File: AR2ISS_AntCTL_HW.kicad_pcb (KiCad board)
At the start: 2 copper layers, 160 x 111.5 mm, 226 parts, among them J1 Conn_01x02, J10 Conn_01x02, J11 Conn_01x02, J12 Conn_01x02, J13 Conn_01x02, J2 Conn_01x04, J3 Conn_02x17_Odd_Even, J4 Conn_02x17_Odd_Even, J5 Conn_02x03_Odd_Even, J6 Conn_01x10, J7 DB9_Female, J8 Conn_01x02, J9 RJ45_LED, K1 G6S-2, Q1 AO3400A, Q2 APM4953KC, Q3 AO3400A, Q4 AO3400A, Q5 AO3400A, Q6 AO3400A, Q7 AO3400A, Q8 AO3400A, Q9 AO3400A, U1 non_plated, U10 74HC164, U11 MCP23017_SO, U12 STM32L522CCTx, U13 SN75176AD, U14 SN75176AD, U15 SN75176AD, U16 SN75176AD, U2 non_plated, U3 non_plated, U4 non_plated, U5 LME78_05-1.0, U6 L78033, U7 TSC101B, U8 MCP23017_SO, U9 TXB0102DCT, Y1 8M

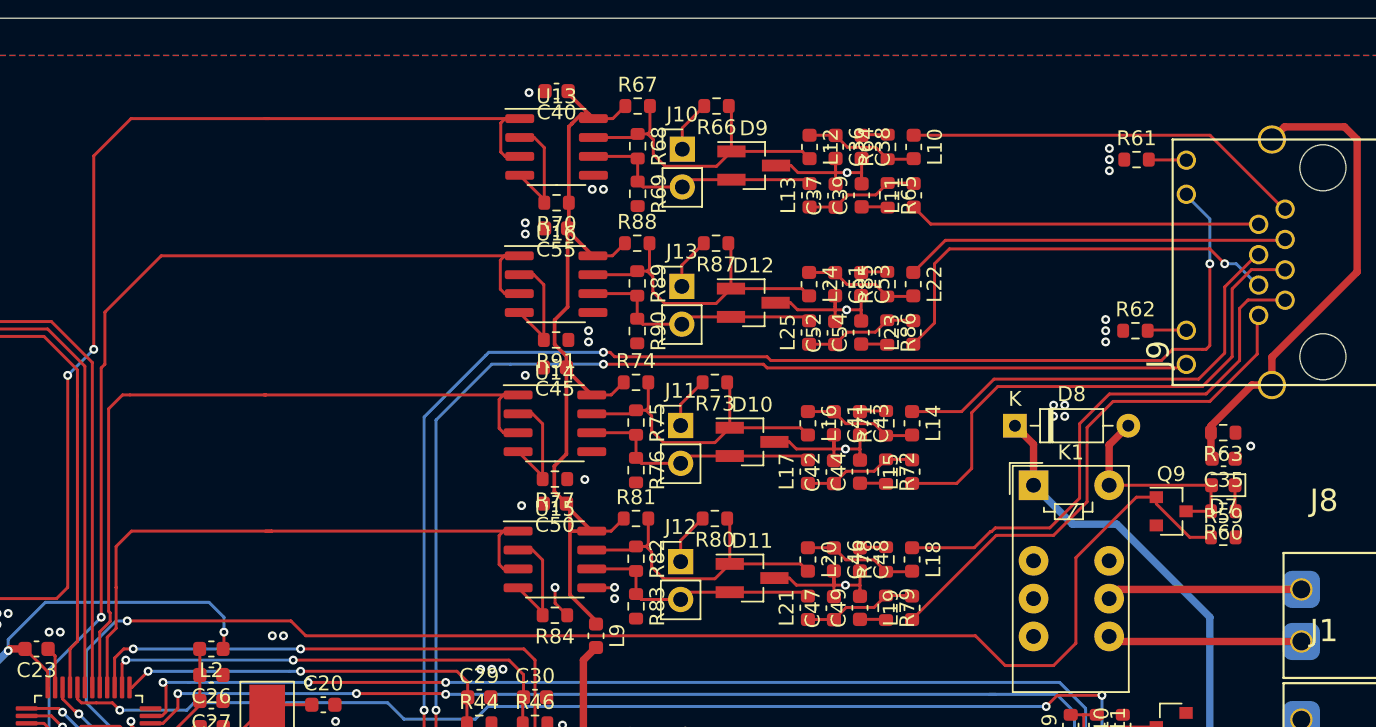
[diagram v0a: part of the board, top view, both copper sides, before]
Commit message: rx tx fix, filter mirrored
switched rx/tx signals
filters were mirrored
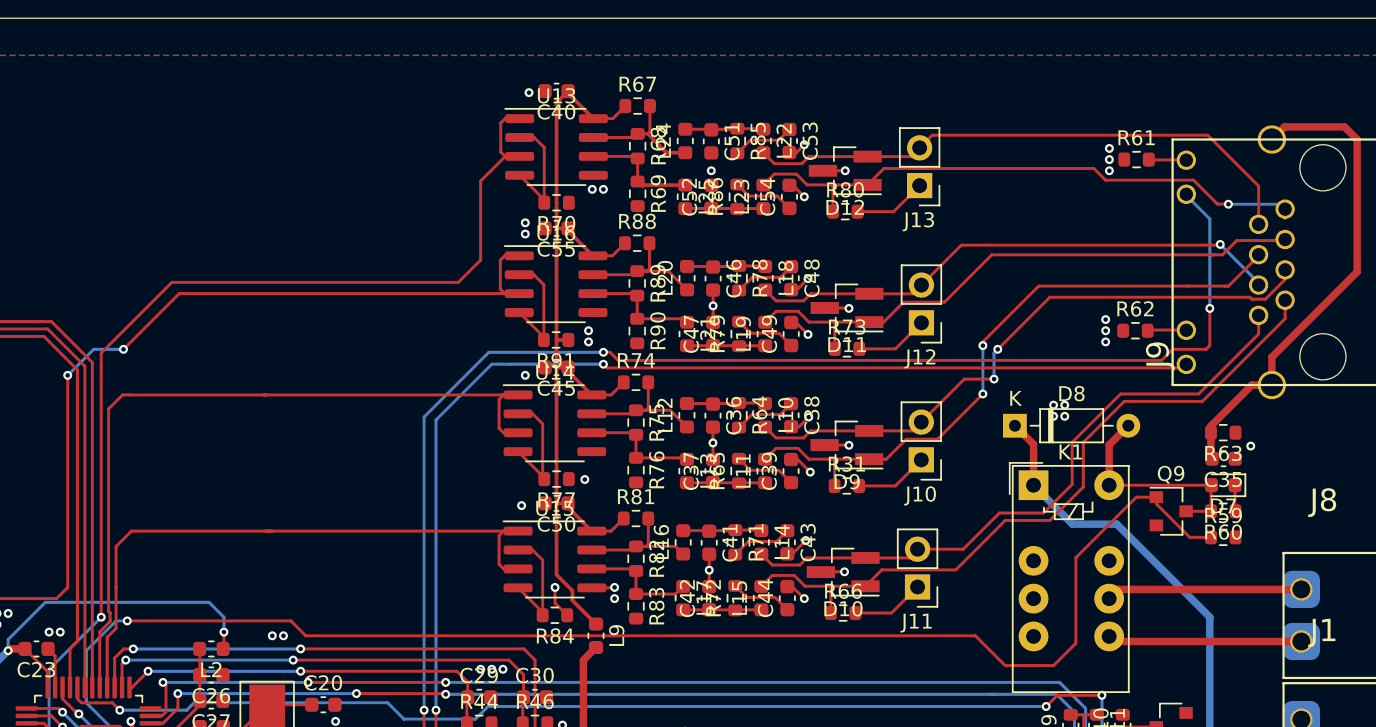
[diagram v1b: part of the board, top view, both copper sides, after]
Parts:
- removed R87: 120, Resistor_SMD:R_0603_1608Metric
- added R31: 120, Resistor_SMD:R_0603_1608Metric, F.Cu at (163.4, 69.9)
- L10, L11, L14, L15, L18, L19, L22, L23: value 10u -> 74279266
- L12, L13, L16, L17, L20, L21, L24, L25: value 74279266 -> 10u
- R64, R65, R71, R72, R78, R79, R85, R86: value 221 -> 220
- moved R66 35.1 mm to (163.1, 78.5), turned to 0 degrees
- moved J10 26.3 mm to (168.4, 68.2), turned to 180 degrees
- moved J12 22.8 mm to (168.4, 59.0), turned to 180 degrees
- moved R80 22.4 mm to (163.2, 51.5), turned to 0 degrees
- moved L18 21.3 mm to (157.9, 56.0)
- moved R78 21.3 mm to (156.1, 56.0), turned to 270 degrees
- moved L11 21.1 mm to (157.9, 68.9)
- moved R65 21.1 mm to (156.1, 68.9), turned to 90 degrees
- moved L19 20.9 mm to (157.9, 59.7)
- moved R79 20.9 mm to (156.1, 59.7), turned to 90 degrees
- moved L10 20.6 mm to (157.9, 65.2)
- moved R64 20.6 mm to (156.1, 65.2), turned to 270 degrees
- moved L20 20.6 mm to (152.6, 56.0), turned to 90 degrees
- moved C46 20.5 mm to (154.4, 56.0)
- moved L13 20.3 mm to (152.6, 68.9), turned to 270 degrees
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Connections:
- C40 pad 1: /RS422/RS485Tranceiver1/MODE -> /RS422/RS485Tranceiver2/MODE
- C45 pad 1: /RS422/RS485Tranceiver1/MODE -> /RS422/RS485Tranceiver2/MODE
- C50 pad 1: /RS422/RS485Tranceiver1/MODE -> /RS422/RS485Tranceiver2/MODE
- C55 pad 1: /RS422/RS485Tranceiver1/MODE -> /RS422/RS485Tranceiver2/MODE
- D10 pad 1: Net-(D10-Pad1) -> /RS422/RS485Tranceiver4/A_in
- D10 pad 2: Net-(D10-Pad2) -> /RS422/RS485Tranceiver4/B_in
- D11 pad 1: Net-(D11-Pad1) -> /RS422/RS485Tranceiver2/A_in
- D11 pad 2: Net-(D11-Pad2) -> /RS422/RS485Tranceiver2/B_in
- D12 pad 1: Net-(D12-Pad1) -> /RS422/RS485Tranceiver1/A_in
- D12 pad 2: Net-(D12-Pad2) -> /RS422/RS485Tranceiver1/B_in
- D9 pad 1: Net-(D9-Pad1) -> /RS422/RS485Tranceiver3/A_in
- D9 pad 2: Net-(D9-Pad2) -> /RS422/RS485Tranceiver3/B_in
- J10 pad 2: Net-(D9-Pad2) -> /RS422/RS485Tranceiver3/B_in
- J11 pad 2: Net-(D10-Pad2) -> /RS422/RS485Tranceiver4/B_in
- J12 pad 2: Net-(D11-Pad2) -> /RS422/RS485Tranceiver2/B_in
- J13 pad 2: Net-(D12-Pad2) -> /RS422/RS485Tranceiver1/B_in
- L10 pad 1: /RS422/RS485Tranceiver1/A_in -> Net-(C36-Pad1)
- L10 pad 2: Net-(C36-Pad1) -> /RS422/RS485Tranceiver3/B_in
- L11 pad 1: /RS422/RS485Tranceiver1/B_in -> Net-(C37-Pad1)
- L11 pad 2: Net-(C37-Pad1) -> /RS422/RS485Tranceiver3/A_in
- L12 pad 1: Net-(C36-Pad1) -> /RS422/RS485Tranceiver3/filter/A_Out
- L12 pad 2: Net-(D9-Pad1) -> Net-(C36-Pad1)
- L13 pad 1: Net-(C37-Pad1) -> /RS422/RS485Tranceiver3/filter/B_Out
- L13 pad 2: Net-(D9-Pad2) -> Net-(C37-Pad1)
- L14 pad 1: /RS422/RS485Tranceiver3/A_in -> Net-(C41-Pad1)
- L14 pad 2: Net-(C41-Pad1) -> /RS422/RS485Tranceiver4/B_in
- L15 pad 1: /RS422/RS485Tranceiver3/B_in -> Net-(C42-Pad1)
- L15 pad 2: Net-(C42-Pad1) -> /RS422/RS485Tranceiver4/A_in
- L16 pad 1: Net-(C41-Pad1) -> /RS422/RS485Tranceiver4/filter/A_Out
- L16 pad 2: Net-(D10-Pad1) -> Net-(C41-Pad1)
- L17 pad 1: Net-(C42-Pad1) -> /RS422/RS485Tranceiver4/filter/B_Out
- L17 pad 2: Net-(D10-Pad2) -> Net-(C42-Pad1)
- L18 pad 1: /RS422/RS485Tranceiver4/A_in -> Net-(C46-Pad1)
- L18 pad 2: Net-(C46-Pad1) -> /RS422/RS485Tranceiver2/B_in
- L19 pad 1: /RS422/RS485Tranceiver4/B_in -> Net-(C47-Pad1)
- L19 pad 2: Net-(C47-Pad1) -> /RS422/RS485Tranceiver2/A_in
- L20 pad 1: Net-(C46-Pad1) -> /RS422/RS485Tranceiver2/filter/A_Out
- L20 pad 2: Net-(D11-Pad1) -> Net-(C46-Pad1)
- L21 pad 1: Net-(C47-Pad1) -> /RS422/RS485Tranceiver2/filter/B_Out
- L21 pad 2: Net-(D11-Pad2) -> Net-(C47-Pad1)
- L22 pad 1: /RS422/RS485Tranceiver2/A_in -> Net-(C51-Pad1)
- L22 pad 2: Net-(C51-Pad1) -> /RS422/RS485Tranceiver1/B_in
- L23 pad 1: /RS422/RS485Tranceiver2/B_in -> Net-(C52-Pad1)
- L23 pad 2: Net-(C52-Pad1) -> /RS422/RS485Tranceiver1/A_in
- L24 pad 1: Net-(C51-Pad1) -> /RS422/RS485Tranceiver1/filter/A_Out
- L24 pad 2: Net-(D12-Pad1) -> Net-(C51-Pad1)
- L25 pad 1: Net-(C52-Pad1) -> /RS422/RS485Tranceiver1/filter/B_Out
- L25 pad 2: Net-(D12-Pad2) -> Net-(C52-Pad1)
- L9 pad 1: /RS422/RS485Tranceiver1/MODE -> /RS422/RS485Tranceiver2/MODE
- R66 pad 1: Net-(D9-Pad1) -> /RS422/RS485Tranceiver4/A_in
- R66 pad 2: Net-(J10-Pad1) -> Net-(J11-Pad1)
- R67 pad 1: /RS422/RS485Tranceiver1/MODE -> /RS422/RS485Tranceiver2/MODE
- R67 pad 2: Net-(D9-Pad1) -> /RS422/RS485Tranceiver1/filter/A_Out
- R68 pad 1: Net-(D9-Pad1) -> /RS422/RS485Tranceiver1/filter/A_Out
- R68 pad 2: Net-(D9-Pad2) -> /RS422/RS485Tranceiver1/filter/B_Out
- R69 pad 1: Net-(D9-Pad2) -> /RS422/RS485Tranceiver1/filter/B_Out
- R70 pad 1: /RS422/RS485Tranceiver1/MODE -> GND
- R73 pad 1: Net-(D10-Pad1) -> /RS422/RS485Tranceiver2/A_in
- R73 pad 2: Net-(J11-Pad1) -> Net-(J12-Pad1)
- R74 pad 1: /RS422/RS485Tranceiver1/MODE -> /RS422/RS485Tranceiver2/MODE
- R74 pad 2: Net-(D10-Pad1) -> /RS422/RS485Tranceiver3/filter/A_Out
- R75 pad 1: Net-(D10-Pad1) -> /RS422/RS485Tranceiver3/filter/A_Out
- R75 pad 2: Net-(D10-Pad2) -> /RS422/RS485Tranceiver3/filter/B_Out
- R76 pad 1: Net-(D10-Pad2) -> /RS422/RS485Tranceiver3/filter/B_Out
- R80 pad 1: Net-(D11-Pad1) -> /RS422/RS485Tranceiver1/A_in
- R80 pad 2: Net-(J12-Pad1) -> Net-(J13-Pad1)
- R81 pad 1: /RS422/RS485Tranceiver1/MODE -> /RS422/RS485Tranceiver2/MODE
- R81 pad 2: Net-(D11-Pad1) -> /RS422/RS485Tranceiver4/filter/A_Out
- R82 pad 1: Net-(D11-Pad1) -> /RS422/RS485Tranceiver4/filter/A_Out
- R82 pad 2: Net-(D11-Pad2) -> /RS422/RS485Tranceiver4/filter/B_Out
- R83 pad 1: Net-(D11-Pad2) -> /RS422/RS485Tranceiver4/filter/B_Out
- R88 pad 1: /RS422/RS485Tranceiver1/MODE -> /RS422/RS485Tranceiver2/MODE
- R88 pad 2: Net-(D12-Pad1) -> /RS422/RS485Tranceiver2/filter/A_Out
- R89 pad 1: Net-(D12-Pad1) -> /RS422/RS485Tranceiver2/filter/A_Out
- R89 pad 2: Net-(D12-Pad2) -> /RS422/RS485Tranceiver2/filter/B_Out
- R90 pad 1: Net-(D12-Pad2) -> /RS422/RS485Tranceiver2/filter/B_Out
- R91 pad 1: GND -> /RS422/RS485Tranceiver2/MODE
- U13 pad 1: /RS422/TX -> /RS422/RX
- U13 pad 3: /RS422/TX -> /RS422/RX
- U13 pad 6: Net-(D9-Pad2) -> /RS422/RS485Tranceiver1/filter/B_Out
- U13 pad 7: Net-(D9-Pad1) -> /RS422/RS485Tranceiver1/filter/A_Out
- U13 pad 8: /RS422/RS485Tranceiver1/MODE -> /RS422/RS485Tranceiver2/MODE
- U14 pad 6: Net-(D10-Pad2) -> /RS422/RS485Tranceiver3/filter/B_Out
- U14 pad 7: Net-(D10-Pad1) -> /RS422/RS485Tranceiver3/filter/A_Out
- U14 pad 8: /RS422/RS485Tranceiver1/MODE -> /RS422/RS485Tranceiver2/MODE
- U15 pad 6: Net-(D11-Pad2) -> /RS422/RS485Tranceiver4/filter/B_Out
- U15 pad 7: Net-(D11-Pad1) -> /RS422/RS485Tranceiver4/filter/A_Out
- U15 pad 8: /RS422/RS485Tranceiver1/MODE -> /RS422/RS485Tranceiver2/MODE
- U16 pad 1: /RS422/RX -> /RS422/TX
- U16 pad 3: /RS422/RX -> /RS422/TX
- U16 pad 6: Net-(D12-Pad2) -> /RS422/RS485Tranceiver2/filter/B_Out
- U16 pad 7: Net-(D12-Pad1) -> /RS422/RS485Tranceiver2/filter/A_Out
- U16 pad 8: /RS422/RS485Tranceiver1/MODE -> /RS422/RS485Tranceiver2/MODE
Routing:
- net /RS422/RS485Tranceiver2/MODE: track 0.00 -> 61.3 mm
- net /RS422/RS485Tranceiver1/MODE: track 59.4 -> 0.00 mm
- net Net-(D9-Pad1): track 21.8 -> 0.00 mm
- net Net-(D12-Pad1): track 21.8 -> 0.00 mm
- net Net-(D11-Pad1): track 21.8 -> 0.00 mm
- net Net-(D10-Pad1): track 21.8 -> 0.00 mm
- net GND: track 79.7 -> 61.5 mm, vias 111 -> 123
- net Net-(D9-Pad2): track 16.9 -> 0.00 mm
- net Net-(D12-Pad2): track 16.9 -> 0.00 mm
- net Net-(D11-Pad2): track 16.9 -> 0.00 mm
- net Net-(D10-Pad2): track 16.9 -> 0.00 mm
- net /RS422/RS485Tranceiver1/B_in: track 23.6 -> 38.4 mm
- net /RS422/RS485Tranceiver2/A_in: track 25.9 -> 39.9 mm
- net /RS422/RS485Tranceiver3/A_in: track 30.2 -> 43.4 mm, vias 0 -> 2
- net /RS422/RS485Tranceiver1/A_in: track 27.0 -> 39.9 mm, vias 0 -> 1
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
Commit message: ready for ordering
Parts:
- D10, D11, D12, D9: value PESD2CAN -> PSM712-LF-T7
- Q2: footprint Package_SO:SO-8_5.3x6.2mm_P1.27mm -> Package_TO_SOT_SMD:SOT-363_SC-70-6_Handsoldering
- R67, R69, R74, R76, R81, R83, R88, R90: value 10k -> NB
- R68, R75, R82, R89: value 1k -> NB
- U13, U14, U15, U16: value SN75176AD -> SN65HVD3082
- moved U2 117.6 mm to (104.0, 47.0)
- moved U4 37.1 mm to (194.0, 142.0)
- moved U3 8.56 mm to (44.0, 47.0)
- moved U1 2.49 mm to (44.0, 142.0)
- moved Q2 1.21 mm to (181.0, 92.3)
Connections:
- Q2 pad 2: Net-(Q2-Pad2) -> Net-(J1-Pad1)
- Q2 pad 3: Net-(C12-Pad2) -> Net-(Q2-Pad3)
- Q2 pad 4: (no net) -> Net-(C12-Pad2)
- Q2 pad 5: (no net) -> Net-(J1-Pad1)
- Q2 pad 6: (no net) -> Net-(J1-Pad1)
- R11 pad 1: Net-(Q2-Pad2) -> Net-(Q2-Pad3)
- R9 pad 2: Net-(Q2-Pad2) -> Net-(Q2-Pad3)
- U13 pad 3: /RS422/RX -> /RS422/RS485Tranceiver1/DE1
- U13 pad 4: /RS422/RS485Tranceiver1/DE1 -> /RS422/RX
- U13 pad 6: /RS422/RS485Tranceiver1/filter/B_Out -> /RS422/RS485Tranceiver1/filter/A_Out
- U13 pad 7: /RS422/RS485Tranceiver1/filter/A_Out -> /RS422/RS485Tranceiver1/filter/B_Out
- U14 pad 3: /RS422/PTT1 -> /RS422/RS485Tranceiver3/DE1
- U14 pad 4: /RS422/RS485Tranceiver3/DE1 -> /RS422/PTT1
- U14 pad 6: /RS422/RS485Tranceiver3/filter/B_Out -> /RS422/RS485Tranceiver3/filter/A_Out
- U14 pad 7: /RS422/RS485Tranceiver3/filter/A_Out -> /RS422/RS485Tranceiver3/filter/B_Out
- U15 pad 3: /RS422/PTT2 -> /RS422/RS485Tranceiver4/DE1
- U15 pad 4: /RS422/RS485Tranceiver4/DE1 -> /RS422/PTT2
- U15 pad 6: /RS422/RS485Tranceiver4/filter/B_Out -> /RS422/RS485Tranceiver4/filter/A_Out
- U15 pad 7: /RS422/RS485Tranceiver4/filter/A_Out -> /RS422/RS485Tranceiver4/filter/B_Out
- U16 pad 3: /RS422/TX -> /RS422/RS485Tranceiver2/DE1
- U16 pad 4: /RS422/RS485Tranceiver2/DE1 -> /RS422/TX
- U16 pad 6: /RS422/RS485Tranceiver2/filter/B_Out -> /RS422/RS485Tranceiver2/filter/A_Out
- U16 pad 7: /RS422/RS485Tranceiver2/filter/A_Out -> /RS422/RS485Tranceiver2/filter/B_Out
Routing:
- net Net-(Q2-Pad2): track 7.91 -> 0.00 mm
- net Net-(Q2-Pad3): track 0.00 -> 7.89 mm
- net Net-(J1-Pad1): track 11.9 -> 17.2 mm
- net Net-(C12-Pad1): track 46.7 -> 51.4 mm
- net /RS422/RS485Tranceiver3/filter/A_Out: track 9.57 -> 13.7 mm
- net /RS422/RS485Tranceiver4/filter/A_Out: track 9.07 -> 13.2 mm
- net /RS422/RS485Tranceiver2/filter/A_Out: track 9.56 -> 13.7 mm
- net /RS422/RS485Tranceiver1/filter/A_Out: track 8.48 -> 12.6 mm
- net /RS422/RS485Tranceiver2/DE1: track 8.17 -> 5.29 mm
- net /RS422/RS485Tranceiver1/DE1: track 8.17 -> 5.29 mm
- net /RS422/RS485Tranceiver3/DE1: track 8.17 -> 5.33 mm
- net /RS422/RS485Tranceiver4/DE1: track 8.17 -> 5.64 mm
- net Net-(C12-Pad2): track 14.7 -> 16.6 mm
- net /RS422/PTT2: track 42.3 -> 42.9 mm
- net /RS422/RS485Tranceiver2/filter/B_Out: track 8.03 -> 8.56 mm
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
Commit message: silkscreen
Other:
- board text added: "1"
- board text added: "Buttons"
- board text added: "Coax Rel 1: NC 2: NO 3: 5V 4: -- 5:-- 6: -- 7: A 8: B 9: 24V"
- board text added: "Debug"
- board text added: "Display + LEDs"
- board text added: "ELE UP DOWN DCOUT --"
- board text added: "F 24V"
- board text added: "F LOGIC"
- board text added: "F PREAMP"
- board text added: "GND GND 12V 24V"
- board text added: "GND Preamp Out"
- board text added: "RIGHT LEFT AZI GND --"
- board text added: "Rel Amp Rel Amp"

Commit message: ready for jlc
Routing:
- net GND: vias 123 -> 358
- net (no net): vias 60 -> 6
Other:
- board text added: "AR2ISS Antenna Control by D04DKW 2021"
- board text added: "BTN8 BTN10 BTN12 BTN4 BTN2 BTN0 GND GND ENC_A GND GND ENC_B 5V GND GND"
- board text added: "D0 D2 D4 CD WE LED22 LED21 LED20 LED18 LED16 LED14 LED12 LED10 LED8 LED6 LED5 LED3"
- board text added: "D1 D3 D5 D7 CE LED9 LED19 LED17 LED15 LED13 LED11 LED7 LED6 LED4 LED2"
- board text added: "LED1 BTN9 BTN11 BTN3 BTN1 GND GND GND GND 5V GND GND"

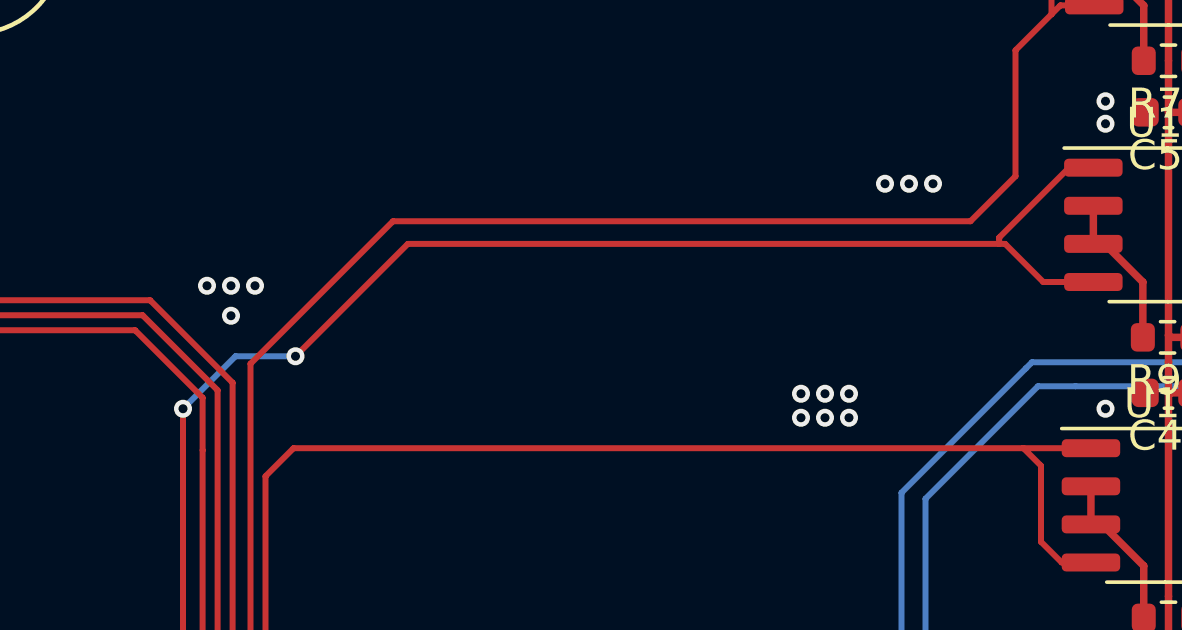
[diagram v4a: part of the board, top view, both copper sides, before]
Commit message: uart rx tx reversed
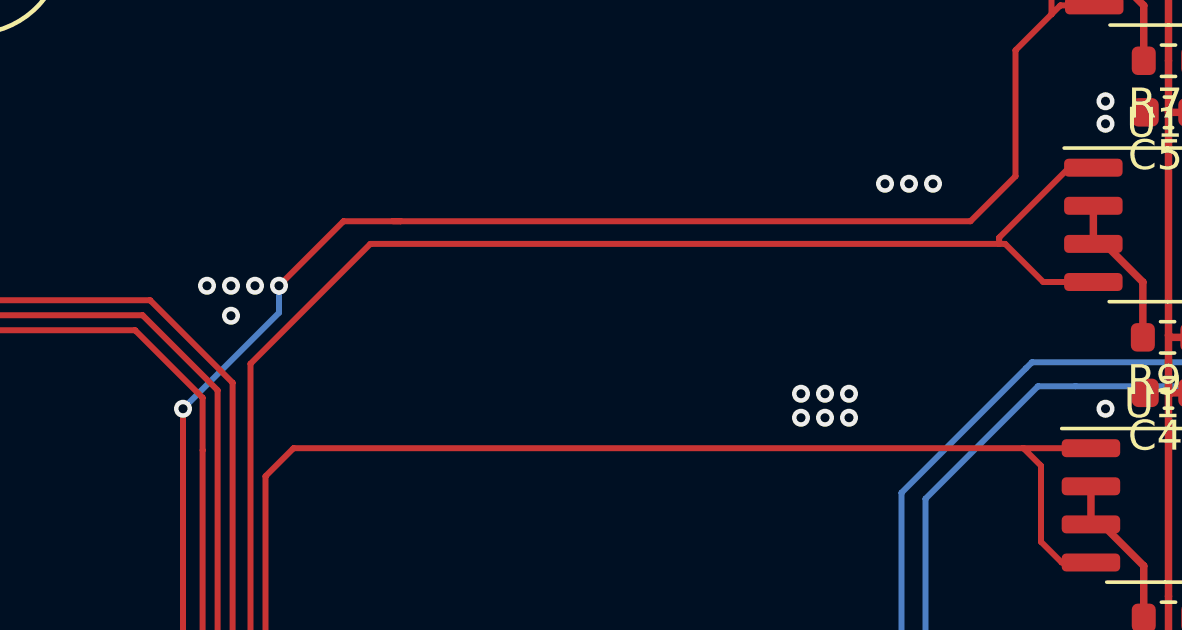
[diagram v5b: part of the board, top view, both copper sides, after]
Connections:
- U12 pad 31: /RS422/TX -> /RS422/RX
- U12 pad 42: /RS422/RX -> /RS422/TX
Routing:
- net /RS422/RX: track 74.0 -> 83.4 mm, vias 2 -> 4
- net /RS422/TX: track 76.4 -> 67.8 mm, vias 4 -> 2
